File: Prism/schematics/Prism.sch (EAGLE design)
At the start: 149 parts, among them IC100 LD1117S50, IC110 LD1117S33, IC3 TL074D, IC4 CS4271, IC5 NE5532D, IC6 NE5532D, IC7 LM317, IC9 N25Q128A13, U1 STM32F405VGT6, X2 53048-05, Y1 24.576MHz, Y2 8MHz

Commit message: Verified analogue circuit and updated values to match other products
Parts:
- added C18, C25: 47n, Rebel:C-EUC0603
- R504, R509: value 20k -> 22k
- R602, R605, R609, R612: value 5k6 -> 4k3
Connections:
- net AOUTA+: now also C25.1
- net AOUTA-: now also C25.2
- net AOUTB+: now also C18.2
- net AOUTB-: now also C18.1
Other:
- moved on the sheet: C603, C604, C608, C609, C610, R602, R605, R609, R612

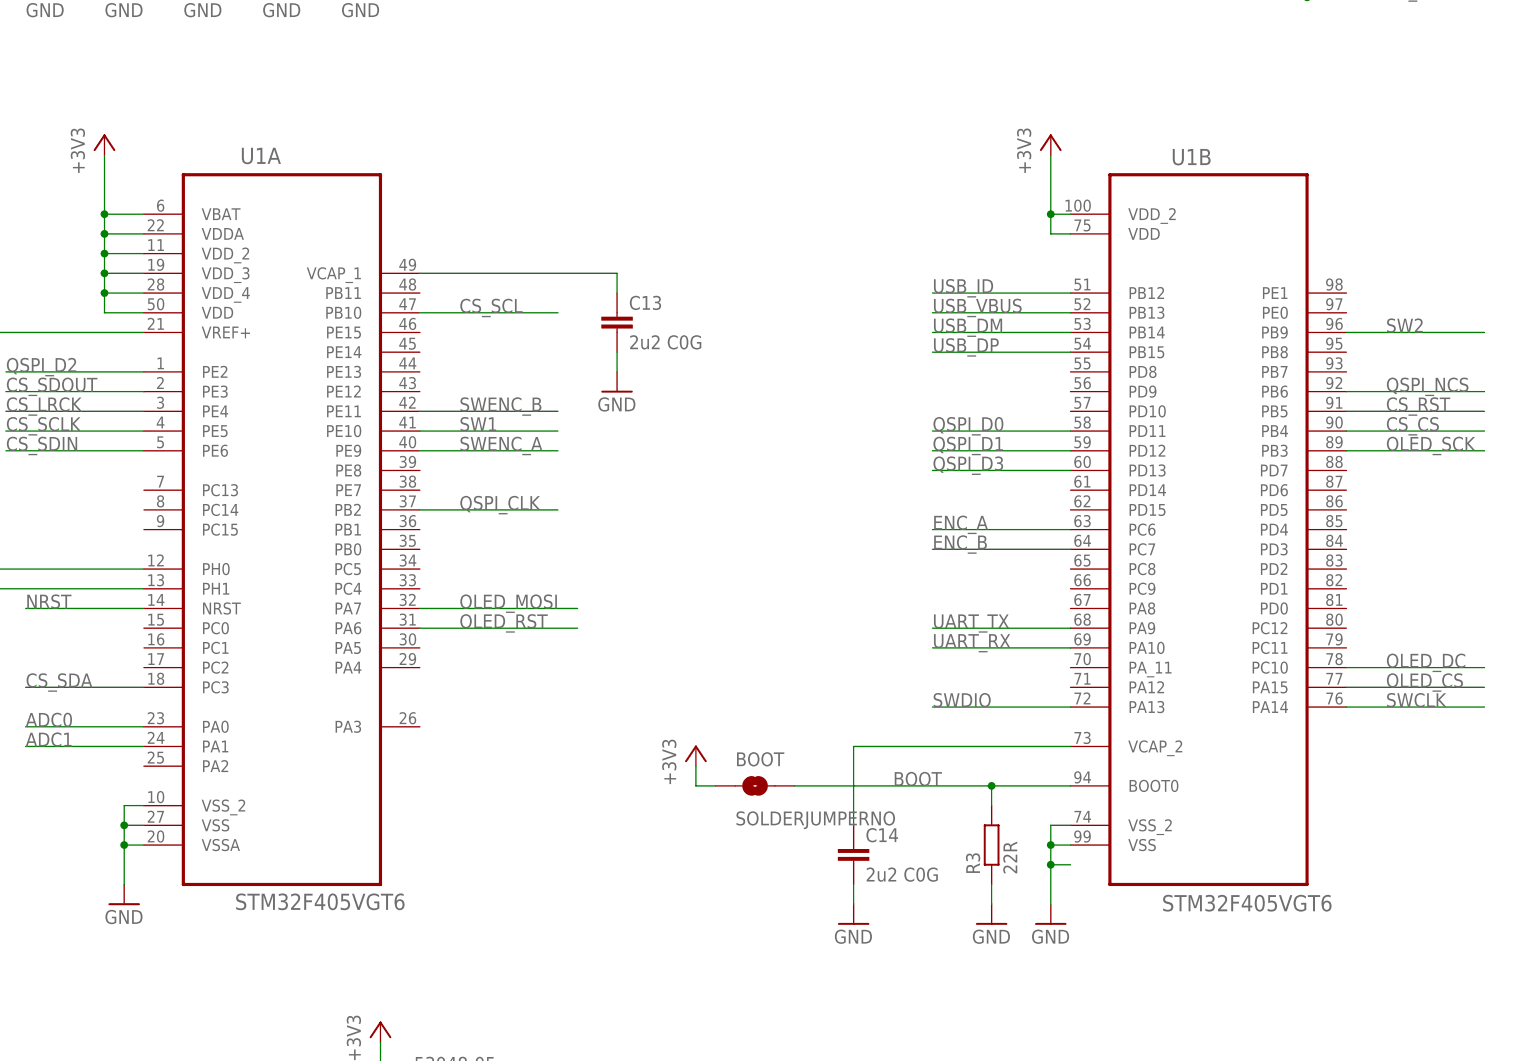
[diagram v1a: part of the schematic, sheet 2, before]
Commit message: Player and Prism updated and changed to F4 MCU part
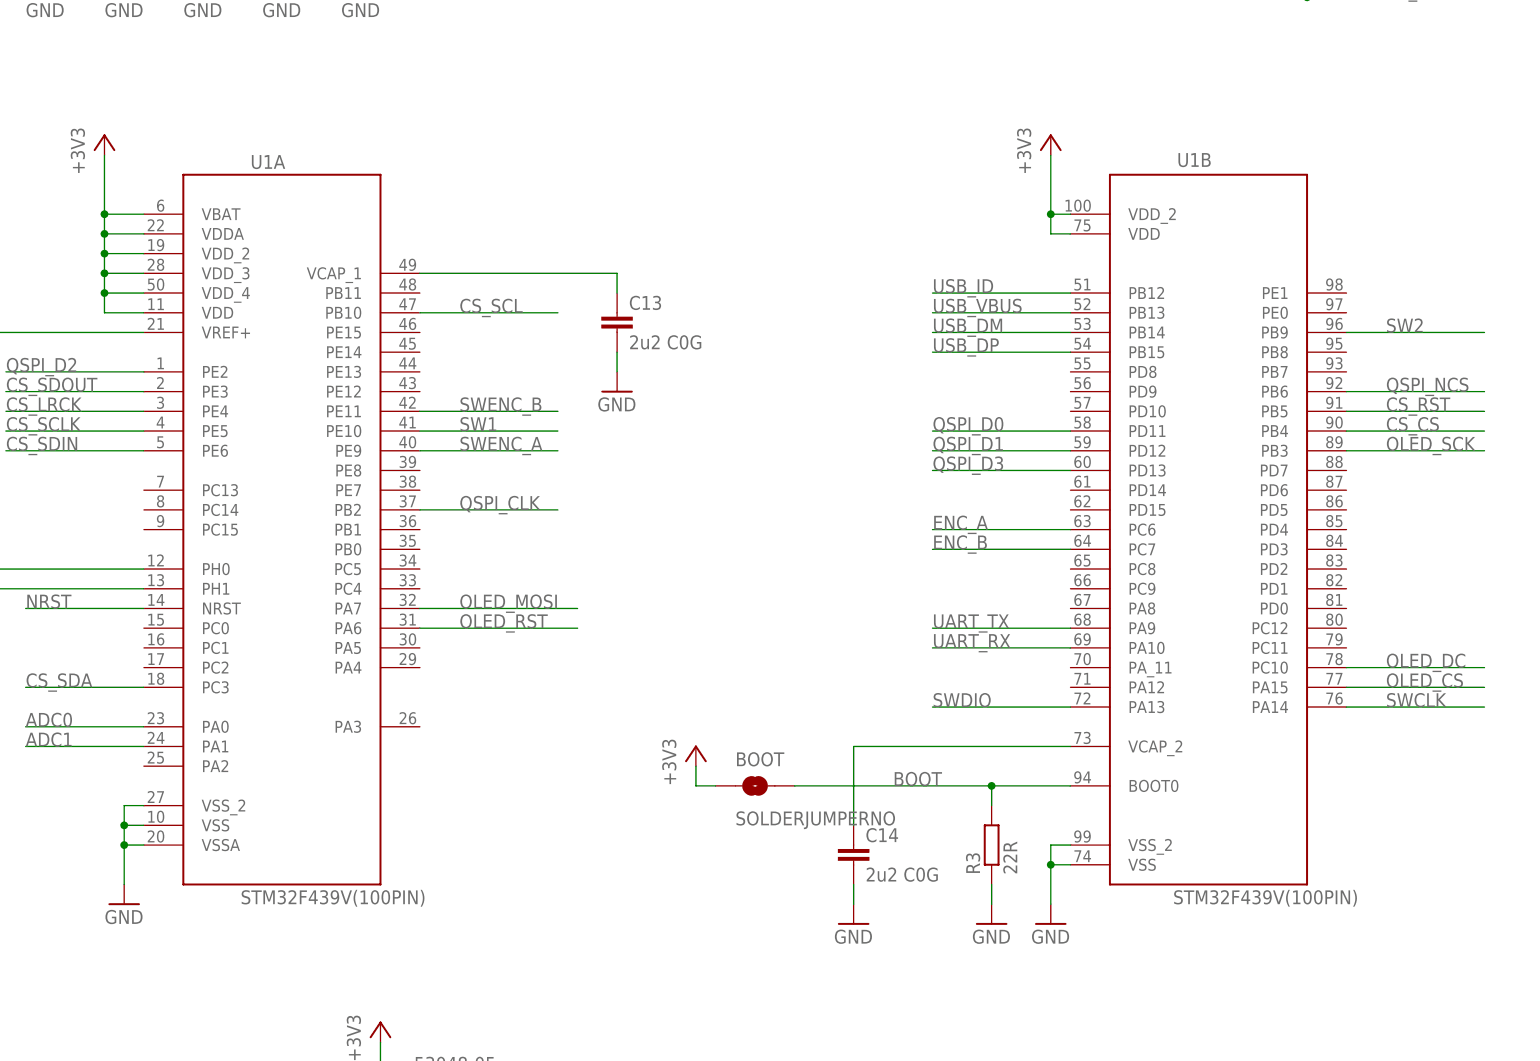
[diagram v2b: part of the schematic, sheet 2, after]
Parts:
- U1: value STM32F405VGT6 -> STM32F439V(100PIN); device Rebel:STM32F405VGT6 -> Rebel:STM32F439V(100PIN)
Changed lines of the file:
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@@
 <?xml version="1.0" encoding="utf-8"?>
 <!DOCTYPE eagle SYSTEM "eagle.dtd">
-<eagle version="6.6.0">
+<eagle version="7.6.0">
 <drawing>
 <settings>
@@
 <layer number="2" name="Route2" color="1" fill="3" visible="no" active="no"/>
 <layer number="3" name="Route3" color="4" fill="3" visible="no" active="no"/>
+<layer number="4" name="Route4" color="1" fill="4" visible="no" active="no"/>
+<layer number="5" name="Route5" color="4" fill="4" visible="no" active="no"/>
+<layer number="6" name="Route6" color="1" fill="8" visible="no" active="no"/>
+<layer number="7" name="Route7" color="4" fill="8" visible="no" active="no"/>
+<layer number="8" name="Route8" color="1" fill="2" visible="no" active="no"/>
+<layer number="9" name="Route9" color="4" fill="2" visible="no" active="no"/>
+<layer number="10" name="Route10" color="1" fill="7" visible="no" active="no"/>
+<layer number="11" name="Route11" color="4" fill="7" visible="no" active="no"/>
+<layer number="12" name="Route12" color="1" fill="5" visible="no" active="no"/>
+<layer number="13" name="Route13" color="4" fill="5" visible="no" active="no"/>
 <layer number="14" name="Route14" color="1" fill="6" visible="no" active="no"/>
 <layer number="15" name="Route15" color="4" fill="6" visible="no" active="no"/>
@@
 <part name="+3V21" library="supply1" deviceset="+3V3" device=""/>
 <part name="GND4" library="supply1" deviceset="GND" device=""/>
-<part name="U1" library="Rebel" deviceset="STM32F405VGT6" device=""/>
+<part name="U1" library="Rebel" deviceset="STM32F439V(100PIN)" device=""/>
 <part name="CN1" library="Rebel" deviceset="CON-JST-1X03" device="PH-TH"/>
 <part name="C18" library="Rebel" deviceset="C-EU" device="C0603" value="47n"/>
@@
 <instance part="P+1" gate="VCC" x="314.96" y="25.4"/>
 <instance part="GND92" gate="1" x="314.96" y="7.62"/>
-<instance part="U1" gate="A" x="116.84" y="121.92"/>
-<instance part="U1" gate="B" x="236.22" y="121.92"/>
+<instance part="U1" gate="A" x="116.84" y="119.38"/>
+<instance part="U1" gate="B" x="236.22" y="119.38"/>
 <instance part="CN1" gate="G$1" x="38.1" y="33.02" rot="R180"/>
 <instance part="C18" gate="G$1" x="436.88" y="121.92"/>
@@
 <wire x1="218.44" y1="76.2" x2="215.9" y2="76.2" width="0.1524" layer="91"/>
 <wire x1="215.9" y1="76.2" x2="215.9" y2="71.12" width="0.1524" layer="91"/>
+<junction x="215.9" y="76.2"/>
 <wire x1="218.44" y1="78.74" x2="215.9" y2="78.74" width="0.1524" layer="91"/>
 <wire x1="215.9" y1="78.74" x2="215.9" y2="76.2" width="0.1524" layer="91"/>
-<junction x="215.9" y="76.2"/>
-<wire x1="218.44" y1="81.28" x2="215.9" y2="81.28" width="0.1524" layer="91"/>
-<wire x1="215.9" y1="81.28" x2="215.9" y2="78.74" width="0.1524" layer="91"/>
-<junction x="215.9" y="78.74"/>
 <pinref part="U1" gate="B" pin="VSS_2"/>
 <pinref part="U1" gate="B" pin="VSS"/>

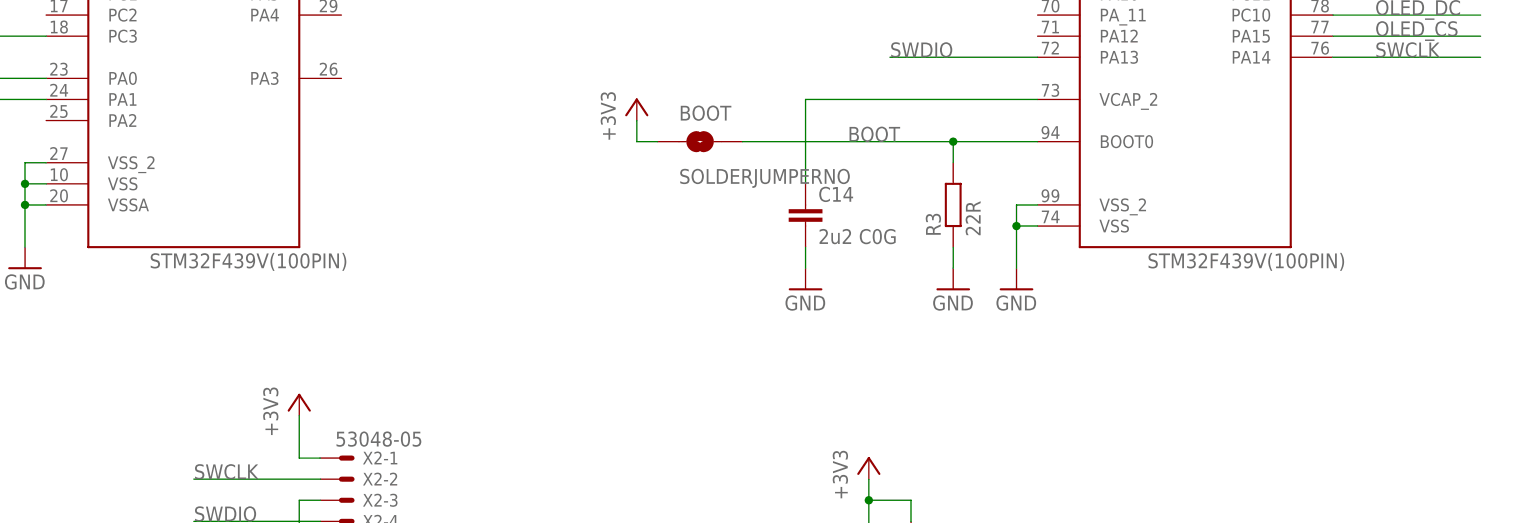
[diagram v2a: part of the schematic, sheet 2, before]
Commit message: Updated Prism and Player MCU to new generic F4 part
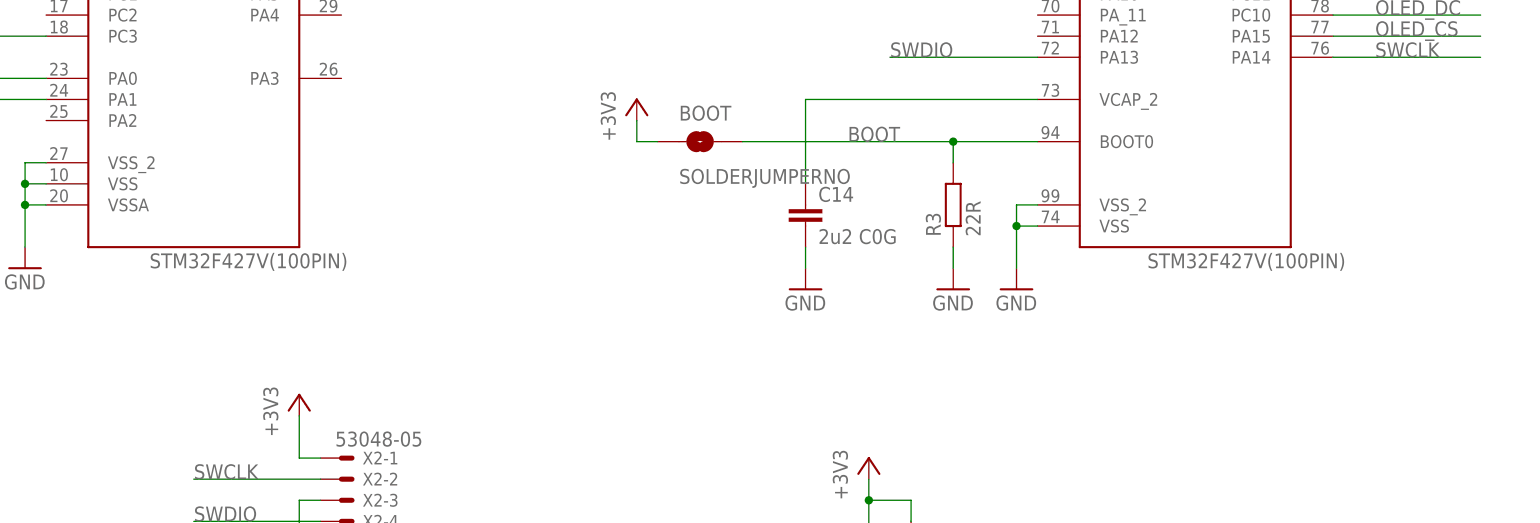
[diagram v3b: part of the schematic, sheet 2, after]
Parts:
- U1: value STM32F439V(100PIN) -> STM32F427V(100PIN); device Rebel:STM32F439V(100PIN) -> Rebel:STM32F42XV/43XV(100PIN)
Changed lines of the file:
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@@
 <part name="+3V21" library="supply1" deviceset="+3V3" device=""/>
 <part name="GND4" library="supply1" deviceset="GND" device=""/>
-<part name="U1" library="Rebel" deviceset="STM32F439V(100PIN)" device=""/>
+<part name="U1" library="Rebel" deviceset="STM32F42XV/43XV(100PIN)" device="" value="STM32F427V(100PIN)"/>
 <part name="CN1" library="Rebel" deviceset="CON-JST-1X03" device="PH-TH"/>
 <part name="C18" library="Rebel" deviceset="C-EU" device="C0603" value="47n"/>
